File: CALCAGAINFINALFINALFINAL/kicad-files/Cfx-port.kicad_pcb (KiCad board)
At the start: 2 copper layers, 65 x 103.5 mm, 133 parts, among them J1 Conn_01x11_Socket, J2 USB_C_Receptacle_USB2.0_16P, J3 Micro_SD_Card, J4 Conn_01x02, SW10 SW_SPST, SW100 SW_SPST, SW101 SW_SPST, SW102 SW_SPST, SW49 SW_SPST, SW52 SW_SPST, SW55 SW_SPST, SW56 SW_SPST, SW57 SW_SPST, SW58 SW_SPST, SW59 SW_SPST, SW60 SW_SPST, SW61 SW_SPST, SW62 SW_SPST, SW63 SW_SPST, SW64 SW_SPST, SW65 SW_SPST, SW66 SW_SPST, SW67 SW_SPST, SW68 SW_SPST, SW69 SW_SPST, SW70 SW_SPST, SW71 SW_SPST, SW72 SW_SPST, SW73 SW_SPST, SW74 SW_SPST, SW75 SW_SPST, SW76 SW_SPST, SW77 SW_SPST, SW78 SW_SPST, SW79 SW_SPST, SW80 SW_SPST, SW81 SW_SPST, SW82 SW_SPST, SW83 SW_SPST, SW84 SW_SPST, SW85 SW_SPST, SW86 SW_SPST, SW87 SW_SPST, SW88 SW_SPST, SW89 SW_SPST, SW90 SW_SPST, SW91 SW_SPST, SW92 SW_SPST, SW93 SW_SPST, SW94 SW_SPST, SW95 SW_SPST, SW96 SW_SPST, SW97 SW_SPST, SW98 SW_SPST, SW99 SW_SPST, U5 TP4056-42-ESOP8, U6 TLV61070ADBV, U7 TCA9535DBR, U8 ESP32-S3-WROOM-1

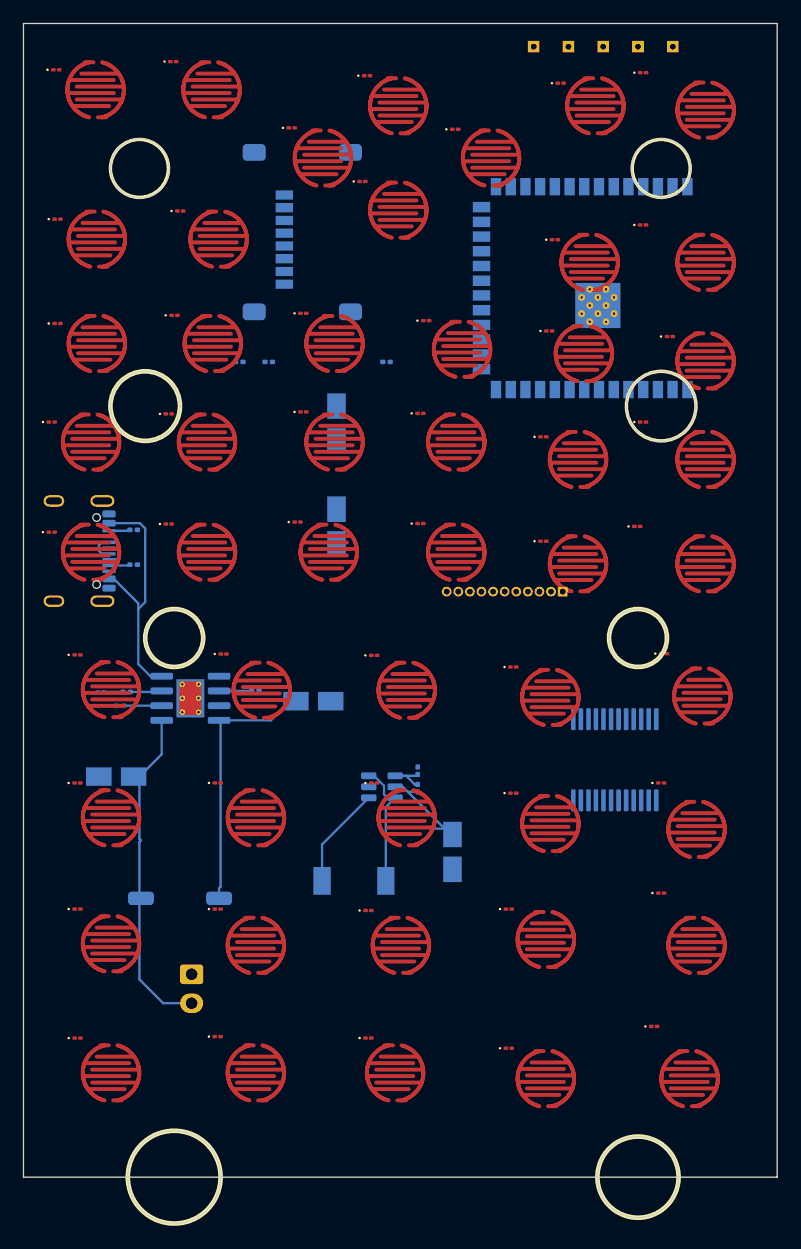
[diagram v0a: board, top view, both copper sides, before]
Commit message: wired rows and cols still need to wire to gpio expander but a gazillion drc errors mean i need to fix them first before i do anything. Next commit is final stretch to compeletion of non camera module then im adding the camera to the schematic and then doin the camera then ordering pcba.
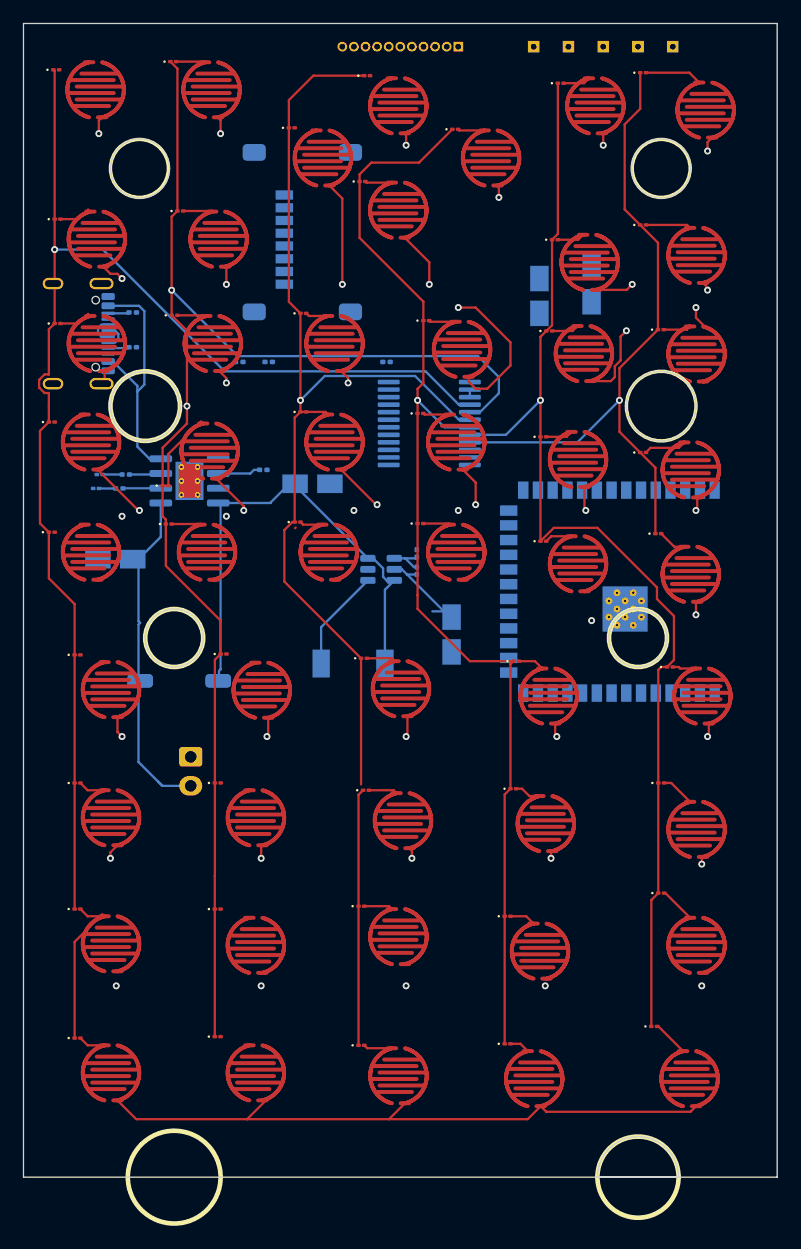
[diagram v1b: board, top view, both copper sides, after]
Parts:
- moved J1 47.9 mm to (107.5, 52.0)
- moved U7 33.1 mm to (105.0, 84.5), turned to 180 degrees
- moved C2 30.3 mm to (119.0, 72.5)
- moved U8 26.3 mm to (124.3, 99.0)
- moved C1 20.7 mm to (114.5, 73.5)
- moved R12 19.0 mm to (90.7, 88.5)
- moved C4 18.8 mm to (94.9, 89.7)
- moved C5 18.8 mm to (77.9, 96.2)
- moved C6 18.8 mm to (106.9, 102.7)
- moved D15 18.8 mm to (76.6, 88.9)
- moved D20 18.8 mm to (76.3, 90.1)
- moved J2 18.8 mm to (73.6, 76.8)
- moved J4 18.8 mm to (84.4, 113.2)
- moved L2 18.8 mm to (98.4, 105.2)
- moved R10 18.8 mm to (78.8, 88.9)
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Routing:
- net /Keypad Matrix/C2: track 0.00 -> 140.9 mm, vias 0 -> 2
- net /Keypad Matrix/C1: track 0.00 -> 140.9 mm, vias 0 -> 1
- net /Keypad Matrix/C3: track 0.00 -> 125.8 mm, vias 0 -> 1
- net /Keypad Matrix/C5: track 0.00 -> 122.7 mm, vias 0 -> 1
- net /Keypad Matrix/C4: track 0.00 -> 116.4 mm, vias 0 -> 1
- net /Keypad Matrix/R3: track 0.00 -> 81.6 mm, vias 0 -> 6
- net /Keypad Matrix/C6: track 0.00 -> 75.9 mm, vias 0 -> 1
- net /Keypad Matrix/R2: track 0.00 -> 72.5 mm, vias 0 -> 6
- net /Keypad Matrix/R5: track 0.00 -> 69.0 mm, vias 0 -> 6
- net /Keypad Matrix/R4: track 0.00 -> 68.9 mm, vias 0 -> 6
- net /Keypad Matrix/R1: track 0.00 -> 66.3 mm, vias 0 -> 6
- net /Keypad Matrix/R6: track 0.00 -> 58.1 mm, vias 0 -> 5
- net /Keypad Matrix/R7: track 0.00 -> 56.4 mm, vias 0 -> 5
- net /Keypad Matrix/R8: track 0.00 -> 56.0 mm, vias 0 -> 5
- net /Keypad Matrix/R9: track 0.00 -> 55.4 mm
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- added copper zone on In2.Cu, net GND
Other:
- board size 65 x 103.5 mm -> 65 x 99.5 mm
- copper layers 2 -> 4

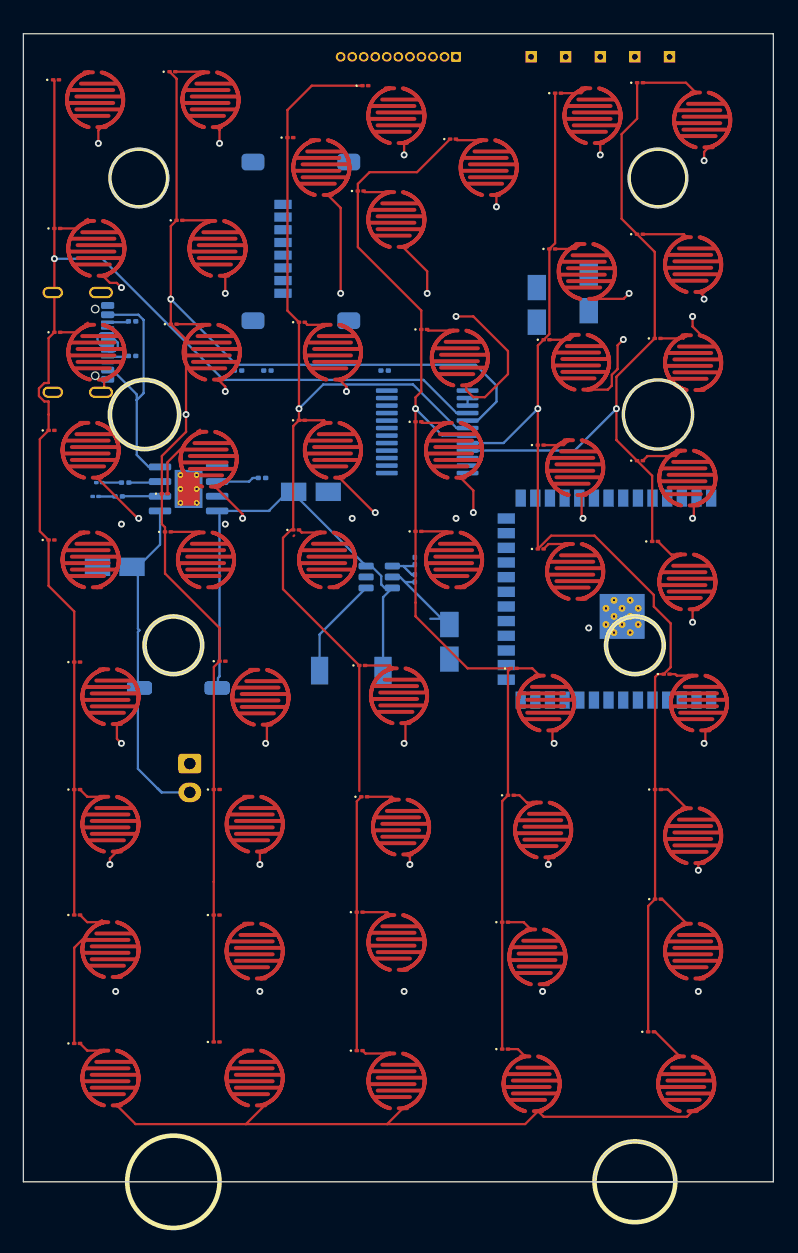
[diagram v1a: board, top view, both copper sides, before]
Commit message: finished button matrix and passed all drc. now need to add tracing for power and data and MC footprints
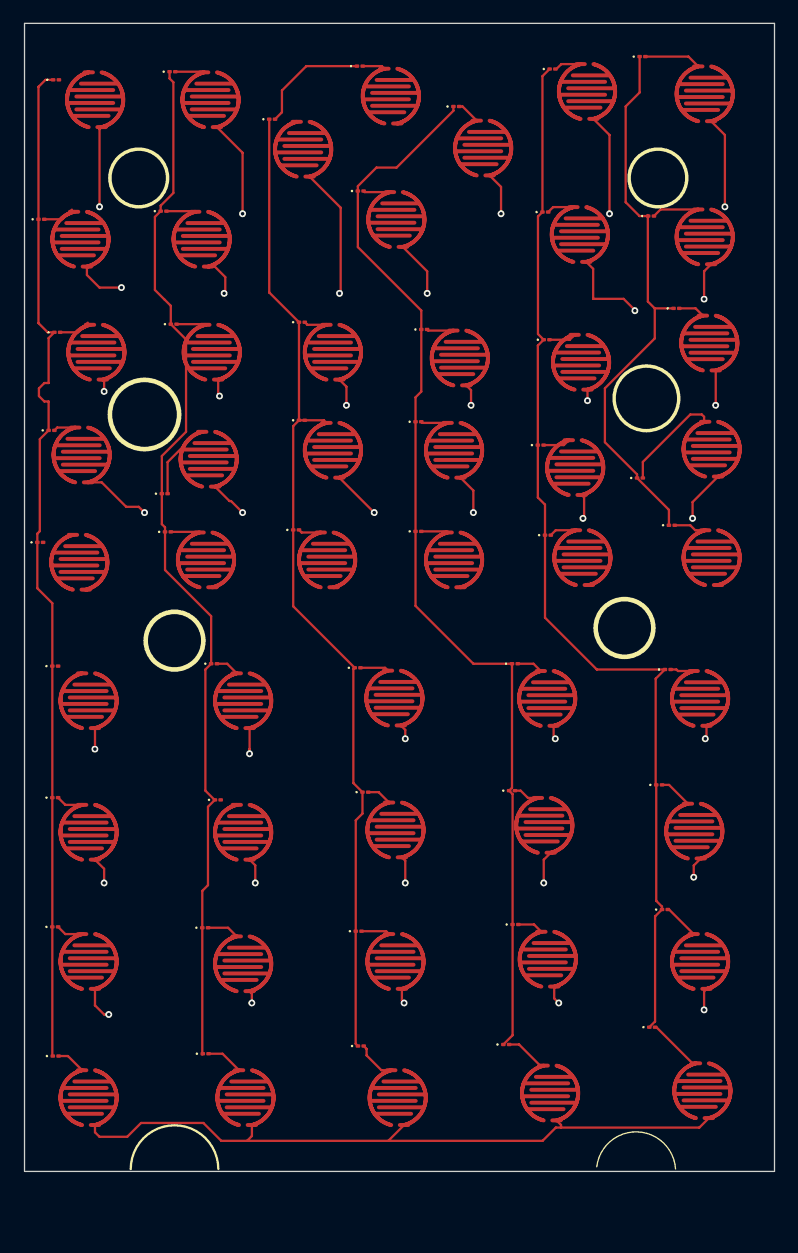
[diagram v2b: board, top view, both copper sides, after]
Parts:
- removed C1, C2: C, Capacitor_SMD:CP_Elec_3x5.3
- removed C4, C5: 10µF, Capacitor_SMD:CP_Elec_3x5.3
- removed C6: 22µF, Capacitor_SMD:CP_Elec_3x5.3
- removed D15, D20: LED, LED_SMD:LED_01005_0402Metric
- removed H1, H2, H3, H4, H5: MountingHole_Pad, TestPoint:TestPoint_THTPad_1.0x1.0mm_Drill0.5mm
- removed J1: Conn_01x11_Socket, Connector_PinSocket_1.00mm:PinSocket_1x11_P1.00mm_Vertical
- removed J2: USB_C_Receptacle_USB2.0_16P, Connector_USB:USB_C_Receptacle_GCT_USB4105-xx-A_16P_TopMnt_Horizontal
- removed J3: Micro_SD_Card, Connector_Card:microSD_HC_Molex_47219-2001
- removed J4: Conn_01x02, Connector_JST:JST_XH_S2B-XH-A-1_1x02_P2.50mm_Horizontal
- removed L2: L, Inductor_SMD:L_6.3x6.3_H3
- removed R1, R10, R11, R12, R2, R3, R9: R, Resistor_SMD:R_0201_0603Metric
- removed R13: 100k, Resistor_SMD:R_0201_0603Metric
- removed R14: 560k, Resistor_SMD:R_0201_0603Metric
- removed R8: 5.1kΩ, Resistor_SMD:R_0201_0603Metric
- removed SW10 (x2): SW_SPST, Button_Switch_SMD:SW_DIP_SPSTx01_Slide_6.7x4.1mm_W6.73mm_P2.54mm_LowProfile_JPin
- removed U5: TP4056-42-ESOP8, Package_SO:SOIC-8-1EP_3.9x4.9mm_P1.27mm_EP2.41x3.3mm_ThermalVias
- removed U6: TLV61070ADBV, Package_TO_SOT_SMD:SOT-23-6
- removed U7: TCA9535DBR, Package_SO:SSOP-24_5.3x8.2mm_P0.65mm
- removed U8: ESP32-S3-WROOM-1, RF_Module:ESP32-S3-WROOM-1
- moved SW101 3.26 mm to (129.6, 86.0)
- moved SW90 3.26 mm to (118.2, 67.4)
- moved D92 3.26 mm to (115.2, 65.5)
- moved D102 3.07 mm to (126.6, 73.8)
- moved SW102 2.97 mm to (129.6, 95.4)
- moved D82 2.84 mm to (107.5, 56.3)
- moved SW99 2.60 mm to (129.0, 67.6)
- moved SW61 2.55 mm to (75.6, 142.2)
- moved D100 2.27 mm to (123.7, 52.0)
- moved SW98 2.27 mm to (129.0, 55.2)
- moved D74 2.24 mm to (91.6, 57.4)
- moved SW72 2.24 mm to (94.2, 60.0)
- moved SW100 2.20 mm to (129.4, 76.8)
- moved SW60 2.16 mm to (75.6, 130.4)
- moved D62 2.16 mm to (72.8, 127.4)
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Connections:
- D82 pad 2: Net-(D82-A) -> /Keypad Matrix/C4
- SW80 pad 2: Net-(D82-A) -> /Keypad Matrix/C4
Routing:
- net /Keypad Matrix/R5: track 69.0 -> 0.00 mm, vias 6 -> 0
- net /power-ic/VBAT_SW: track 42.8 -> 0.00 mm
- net /Keypad Matrix/C1: track 140.9 -> 103.3 mm, vias 1 -> 0
- net VCC: track 30.6 -> 0.00 mm
- net /power-ic/BAT+: track 29.1 -> 0.00 mm
- net /Keypad Matrix/C2: track 140.9 -> 115.0 mm, vias 2 -> 0
- net /Keypad Matrix/R1: track 66.3 -> 90.5 mm, vias 6 -> 5
- net /Keypad Matrix/R2: track 72.5 -> 86.1 mm
- net /Keypad Matrix/R3: track 81.6 -> 68.5 mm
- net /Keypad Matrix/C3: track 125.8 -> 113.8 mm, vias 1 -> 0
- net /Keypad Matrix/R6: track 58.1 -> 68.0 mm
- net Net-(U6-SW): track 8.84 -> 0.00 mm
- net /Keypad Matrix/R8: track 56.0 -> 64.1 mm
- net /Keypad Matrix/R7: track 56.4 -> 63.0 mm
- net /Keypad Matrix/C5: track 122.7 -> 117.2 mm, vias 1 -> 0
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- removed copper zone on In2.Cu, net GND
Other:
- outline, holes or cut-outs redrawn

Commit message: 90%done with pcb need to update footprints to match jlcpcb standard parts and then add camera should be done in ~5 hours there was a bunch of connection not done errors but it wasnt showing them arrow things so ill have to look into that. fixed all clearance related errors tho
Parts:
- added C1: C, Capacitor_SMD:C_1812_4532Metric, B.Cu at (140.6, 79.5)
- added C2: C, Capacitor_SMD:C_1812_4532Metric, B.Cu at (140.8, 87.0)
- added C4: 10µF, Capacitor_SMD:C_1812_4532Metric, B.Cu at (149.1, 67.5)
- added C5: 10µF, Capacitor_SMD:C_1812_4532Metric, B.Cu at (148.8, 74.7)
- added C6: 22µF, Capacitor_SMD:C_1812_4532Metric, B.Cu at (165.8, 79.0)
- added D15: LED, LED_SMD:LED_01005_0402Metric, B.Cu at (130.8, 69.2)
- added H1: MountingHole_Pad, TestPoint:TestPoint_THTPad_1.0x1.0mm_Drill0.5mm, B.Cu at (141.2, 51.1)
- added H2: MountingHole_Pad, TestPoint:TestPoint_THTPad_1.0x1.0mm_Drill0.5mm, B.Cu at (144.2, 51.1)
- added H3: MountingHole_Pad, TestPoint:TestPoint_THTPad_1.0x1.0mm_Drill0.5mm, B.Cu at (147.2, 51.1)
- added H4: MountingHole_Pad, TestPoint:TestPoint_THTPad_1.0x1.0mm_Drill0.5mm, B.Cu at (150.2, 51.1)
- added H5: MountingHole_Pad, TestPoint:TestPoint_THTPad_1.0x1.0mm_Drill0.5mm, B.Cu at (153.2, 51.1)
- added J1: Conn_01x11_Socket, Connector_PinSocket_1.00mm:PinSocket_1x11_P1.00mm_Vertical, B.Cu at (134.7, 51.1)
- added J2: USB_C_Receptacle_USB2.0_16P, Connector_USB:USB_C_Receptacle_GCT_USB4105-xx-A_16P_TopMnt_Horizontal, B.Cu at (120.2, 68.3)
- added J3: Micro_SD_Card, Connector_Card:microSD_HC_Molex_47219-2001, B.Cu at (128.1, 83.4)
- added J4: Conn_01x02, Connector_JST:JST_XH_S2B-XH-A-1_1x02_P2.50mm_Horizontal, B.Cu at (158.7, 102.3)
- added L2: L, Capacitor_SMD:C_1812_4532Metric, B.Cu at (165.6, 87.0)
- added R1: R, Resistor_SMD:R_0201_0603Metric, B.Cu at (119.4, 82.8)
- added R10: R, Resistor_SMD:R_0201_0603Metric, B.Cu at (132.8, 69.2)
- added R11: R, Resistor_SMD:R_0201_0603Metric, B.Cu at (132.8, 70.4)
- added R12: R, Resistor_SMD:R_0201_0603Metric, B.Cu at (143.2, 69.1)
- added R13: 100k, Resistor_SMD:R_0201_0603Metric, B.Cu at (155.6, 81.6)
- added R14: 560k, Resistor_SMD:R_0201_0603Metric, B.Cu at (157.8, 81.6)
- added R2: R, Resistor_SMD:R_0201_0603Metric, B.Cu at (119.4, 86.8)
- added R3: R, Resistor_SMD:R_0201_0603Metric, B.Cu at (119.3, 81.4)
- added R8: 5.1kΩ, Resistor_SMD:R_0201_0603Metric, B.Cu at (125.7, 69.7)
- added R9: R, Resistor_SMD:R_0201_0603Metric, B.Cu at (125.7, 66.7)
- added SW10 (x2): SW_SPST, Button_Switch_SMD:SW_DIP_SPSTx01_Slide_6.7x4.1mm_W6.73mm_P2.54mm_LowProfile_JPin, B.Cu at (149.6, 83.5)
- added U5: TP4056-42-ESOP8, Package_SO:SOIC-8-1EP_3.9x4.9mm_P1.27mm_EP2.41x3.3mm_ThermalVias, B.Cu at (138.0, 69.7)
- added U6: TLV61070ADBV, Package_TO_SOT_SMD:SOT-23-6, B.Cu at (157.7, 84.7)
- added U7: TCA9535DBR, Package_SO:SSOP-24_5.3x8.2mm_P0.65mm, B.Cu at (170.3, 103.1)
- added U8: ESP32-S3-WROOM-1, RF_Module:ESP32-S3-WROOM-1, B.Cu at (168.2, 61.3)
- moved D100 46.1 mm to (169.8, 52.5)
- moved D102 46.1 mm to (172.7, 74.3)
- moved D55 46.1 mm to (118.9, 54.5)
- moved D59 46.1 mm to (117.6, 94.6)
- moved D64 46.1 mm to (129.0, 53.8)
- moved D67 46.1 mm to (128.4, 90.4)
- moved D70 46.1 mm to (133.0, 116.9)
- moved D73 46.1 mm to (145.3, 53.3)
- moved D80 46.1 mm to (145.2, 128.3)
- moved D87 46.1 mm to (158.7, 105.1)
- moved D88 46.1 mm to (158.5, 116.1)
- moved D90 46.1 mm to (158.0, 138.1)
- moved D93 46.1 mm to (161.5, 77.0)
- moved D96 46.1 mm to (172.0, 105.6)
- moved D97 46.1 mm to (171.2, 115.6)
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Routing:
- net /Keypad Matrix/C1: track 103.3 -> 159.8 mm, vias 0 -> 1
- net /Keypad Matrix/C2: track 115.0 -> 162.3 mm, vias 0 -> 1
- net /Keypad Matrix/R9: track 60.2 -> 100.4 mm, vias 0 -> 1
- net /Keypad Matrix/R2: track 86.1 -> 125.8 mm
- net /Keypad Matrix/C3: track 113.8 -> 150.3 mm, vias 0 -> 1
- net /Keypad Matrix/R1: track 90.5 -> 126.4 mm
- net /Keypad Matrix/R8: track 64.1 -> 94.7 mm
- net VCC: track 0.00 -> 28.3 mm
- net /Keypad Matrix/C4: track 115.8 -> 142.0 mm, vias 0 -> 1
- net /Keypad Matrix/R3: track 68.5 -> 93.6 mm
- net /power-ic/VBAT_SW: track 0.00 -> 18.8 mm
- net /Keypad Matrix/R7: track 63.0 -> 81.4 mm
- net /Keypad Matrix/C5: track 117.2 -> 133.6 mm, vias 0 -> 1
- net GND: track 0.00 -> 16.2 mm
- net /power-ic/BAT+: track 0.00 -> 14.1 mm
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
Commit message: dude this bitch ass project is the fucking boulder of sisyphus omfg ima genuinely kms at this rate if this iteration doesnt work ima genuinely kms like acutal this one is bare esp32 s3 with a diy antenna and crystal like dude what the actual fuck man ima genuinely dei. FINAL FINAL FINAL FINAL ITS GOT THE FUCKING BARE CHIPS FOR DAMN NEAR EVERYTHING DEAR MASS PRODUCED CHINK FACTORY GODS LET THIS THROUGH WITHOUT CAUSING A RUCKUS AND CHARGING LIKE $90 FOR 14 BUCKS OF PARTS AMEN
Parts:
- removed D100, D101, D102, D103, D104, D55, D56, D57, D58, D59, D60, D61, D62, D63, D64, D65, D66, D67, D68, D69, D70, D71, D72, D73, D74, D75, D76, D77, D78, D79, D80, D81, D82, D83, D84, D85, D86, D87, D88, D89, D90, D91, D92, D93, D94, D95, D96, D97, D98, D99: 1N4001, Diode_SMD:D_01005_0402Metric
- removed H1, H2, H3, H4, H5: MountingHole_Pad, TestPoint:TestPoint_THTPad_1.0x1.0mm_Drill0.5mm
- removed J1: Conn_01x11_Socket, Connector_PinSocket_1.00mm:PinSocket_1x11_P1.00mm_Vertical
- removed SW10 (x2): SW_SPST, Button_Switch_SMD:SW_DIP_SPSTx01_Slide_6.7x4.1mm_W6.73mm_P2.54mm_LowProfile_JPin
- removed U8: ESP32-S3-WROOM-1, RF_Module:ESP32-S3-WROOM-1
- added REF**: Texas_SWRA117D_2.4GHz_Right, RF_Antenna:Texas_SWRA117D_2.4GHz_Right, F.Cu at (156.1, 37.4)
- added REF**: Omron_XF2M-4015-1A_1x40-1MP_P0.5mm_Horizontal, Connector_FFC-FPC:Omron_XF2M-4015-1A_1x40-1MP_P0.5mm_Horizontal, B.Cu at (105.1, 44.5)
- added REF1: ESP32-S3R8, ButtonPads:QFN40P700X700X90-57N, B.Cu at (144.0, 44.2)
- moved L2 60.6 mm to (106.3, 74.6), turned to 0 degrees
- moved C6 59.8 mm to (106.1, 82.6), turned to 0 degrees
- moved J4 56.5 mm to (103.5, 114.5), turned to -90 degrees
- moved U6 44.1 mm to (114.3, 77.0), turned to -90 degrees
- moved R14 43.3 mm to (114.5, 80.2), turned to 90 degrees
- moved R13 39.3 mm to (116.3, 80.1), turned to 0 degrees
- moved J2 32.8 mm to (101.8, 95.5)
- moved R8 32.1 mm to (109.3, 97.3)
- moved R9 32.0 mm to (109.5, 94.3)
- moved D15 30.7 mm to (112.9, 94.1)
- moved R10 30.7 mm to (114.9, 94.1)
- moved R11 30.7 mm to (114.9, 95.3)
- moved R12 29.2 mm to (128.1, 94.1)
- moved U5 28.9 mm to (123.2, 94.5)
- moved C4 27.5 mm to (137.4, 92.3)
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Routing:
- net /Keypad Matrix/C4: track 142.0 -> 26.7 mm, vias 1 -> 0
- net /Keypad Matrix/C2: track 162.3 -> 47.4 mm, vias 1 -> 0
- net /Keypad Matrix/C3: track 150.3 -> 37.1 mm, vias 1 -> 0
- net /Keypad Matrix/C1: track 159.8 -> 56.1 mm, vias 1 -> 0
- net /Keypad Matrix/R1: track 126.4 -> 27.8 mm, vias 5 -> 1
- net /Keypad Matrix/C6: track 80.2 -> 8.69 mm, vias 1 -> 0
- net /Keypad Matrix/R6: track 74.6 -> 6.63 mm, vias 5 -> 1
- net GND: track 16.2 -> 76.5 mm, vias 0 -> 3
- net /Keypad Matrix/R9: track 100.4 -> 40.2 mm
- net /Keypad Matrix/R4: track 71.6 -> 16.3 mm, vias 6 -> 0
- net /Keypad Matrix/R2: track 125.8 -> 93.7 mm, vias 6 -> 2
- net /Keypad Matrix/R7: track 81.4 -> 67.6 mm
- net /Keypad Matrix/R3: track 93.6 -> 82.7 mm, vias 6 -> 4
- net /Keypad Matrix/R8: track 94.7 -> 85.9 mm
- net /power-ic/VBAT_SW: track 18.8 -> 25.8 mm
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- added copper zone on In2.Cu, net GND
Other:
- board size 65 x 99.5 mm -> 65 x 140 mm
- board text added: "1.fix diode removal 2.add camera connector finalise pinout"
- board text added: "3000mah bat"
